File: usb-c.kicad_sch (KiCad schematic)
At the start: 10 parts, among them IC1 TCPP01-M12, IC2 USBLC6-2SC6, IC3 632723100011, Q1 STL11N3LLH6

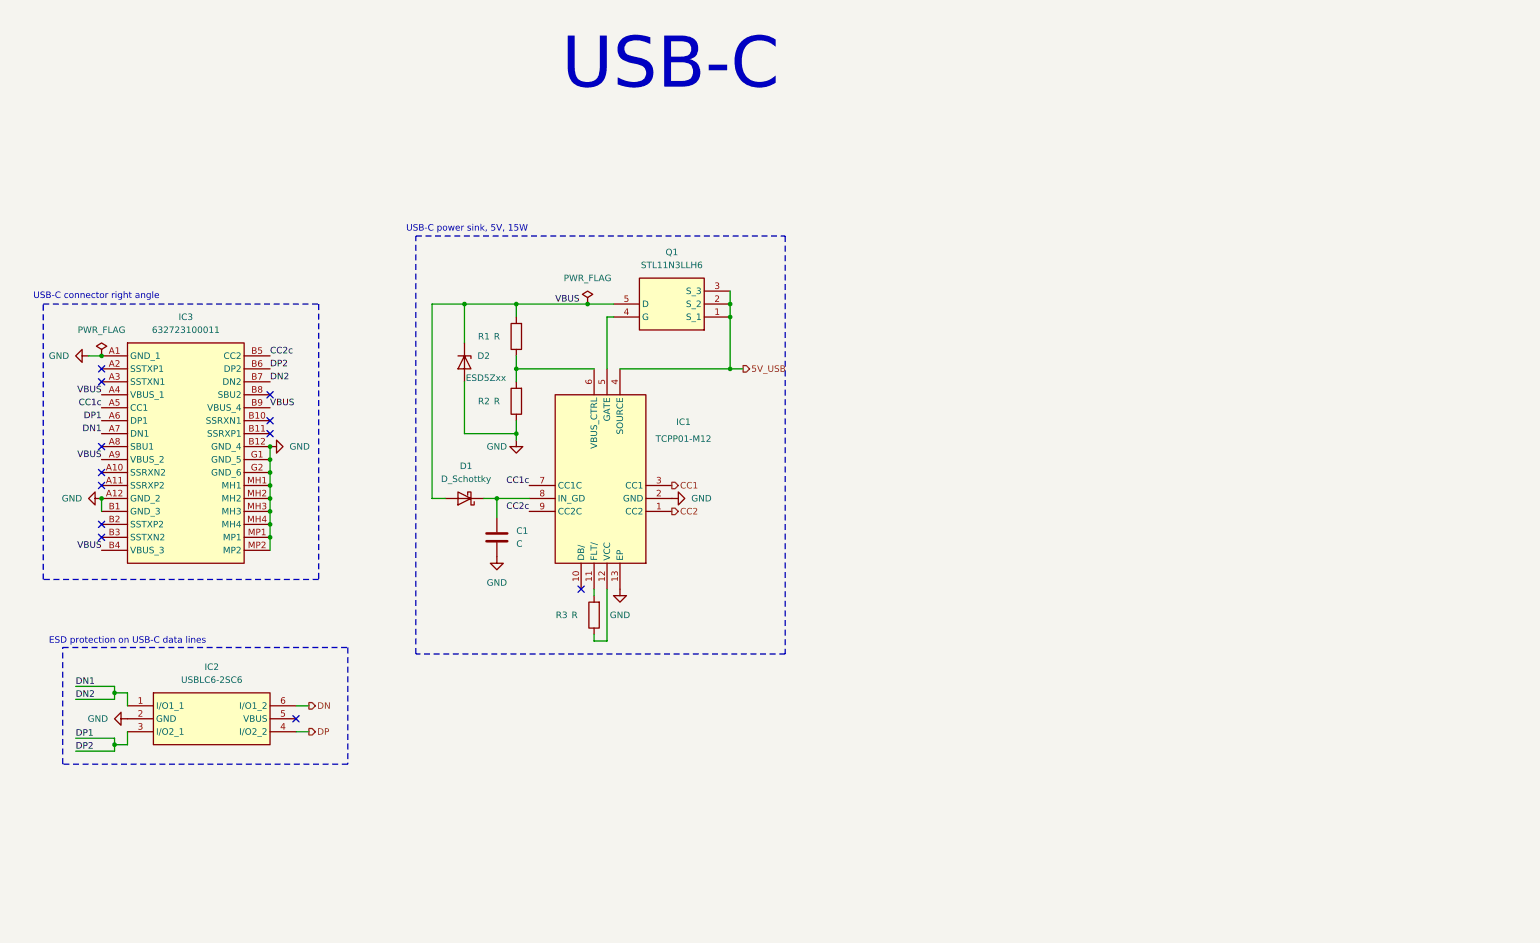
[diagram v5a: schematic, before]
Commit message: Connect all pins to MCU
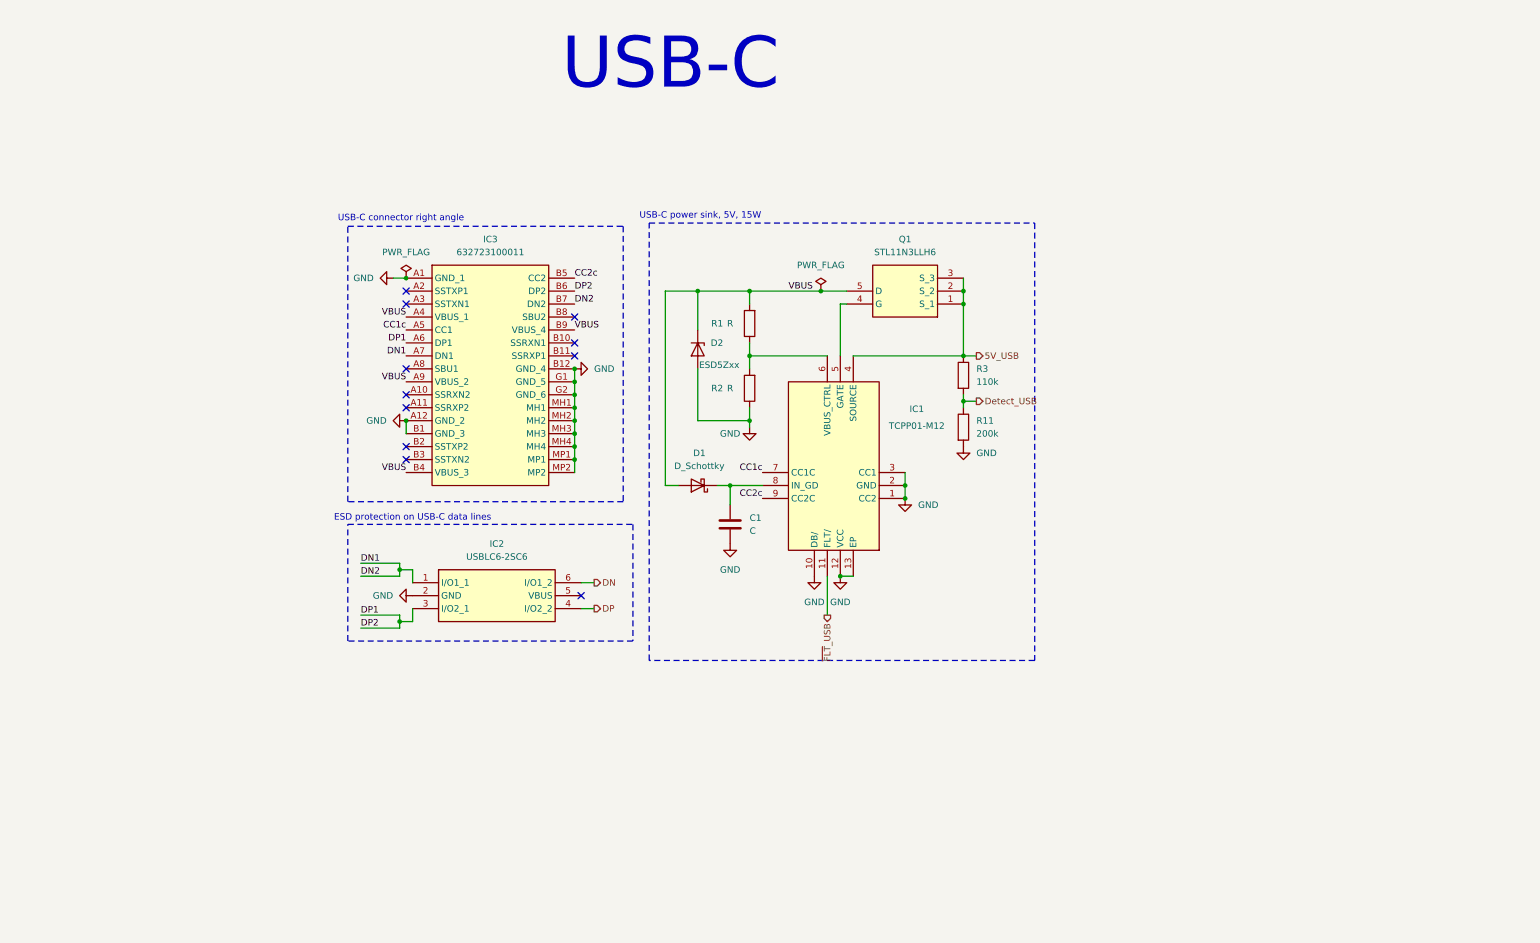
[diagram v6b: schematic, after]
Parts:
- added R11: 200k, symbol Device:R
- R3: value R -> 110k; footprint Resistor_SMD:R_0603_1608Metric_Pad0.98x0.95mm_HandSolder -> (none)
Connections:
- net CC1 is gone; now on net GND: IC1.3 (CC1)
- net CC2 is gone; now on net GND: IC1.1 (CC2)
- net 5V_USB: now also R3.1
- net GND: now also IC1.10 (DB/), IC1.12 (VCC), R11.2
- net Detect_USB: now reaches R3.2
- net Detect_USB: now also R11.1; no longer IC1.11 (FLT/)
- new net ~{FLT}_USB: IC1.11 (FLT/)
- no-connect marks 12 -> 11
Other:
- moved on the sheet: C1, D1, D2, IC1, IC2, IC3, Q1, R1, R2

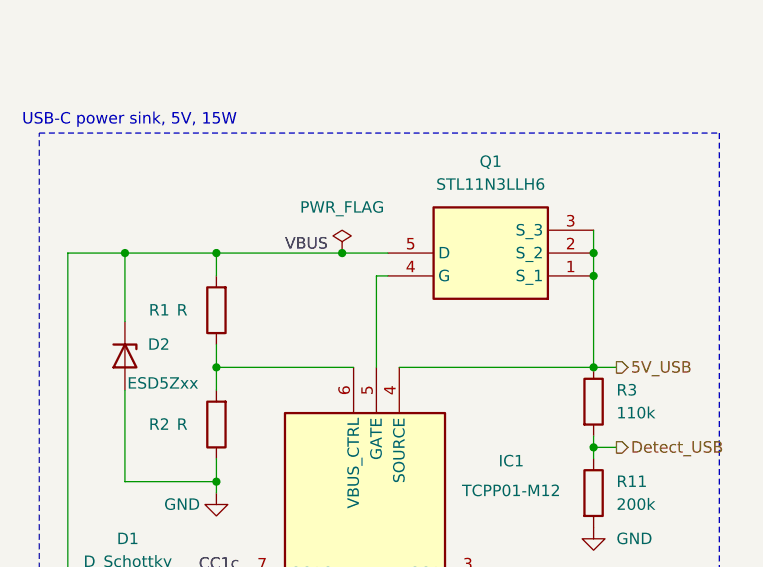
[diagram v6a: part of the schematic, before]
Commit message: Fix some ERC errors
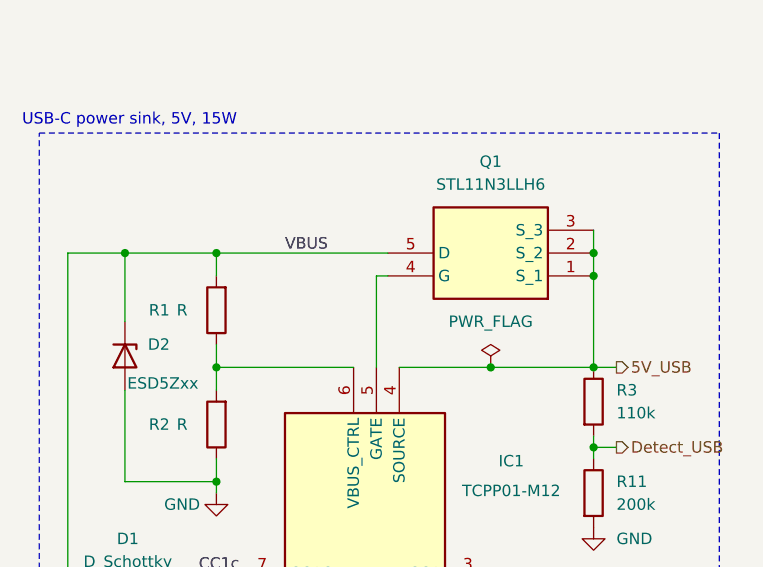
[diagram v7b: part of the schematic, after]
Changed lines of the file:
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@@
+	)
+	(junction
+		(at 191.77 81.28)
+		(diameter 0)
+		(color 0 0 0 0)
 	)
 	(junction
@@
 	)
 	(junction
-		(at 175.26 68.58)
-		(diameter 0)
-		(color 0 0 0 0)
-	)
-	(junction
 		(at 127 83.82)
 		(diameter 0)
@@
 	(wire
 		(pts
-			(xy 175.26 68.58) (xy 180.34 68.58)
-		)
-		(stroke
-			(width 0)
-			(type default)
-		)
-	)
-	(wire
-		(pts
 			(xy 179.07 71.12) (xy 180.34 71.12)
 		)
@@
 	(wire
 		(pts
-			(xy 161.29 68.58) (xy 175.26 68.58)
+			(xy 161.29 68.58) (xy 180.34 68.58)
 		)
 		(stroke
@@
 	(wire
 		(pts
-			(xy 181.61 81.28) (xy 203.2 81.28)
+			(xy 181.61 81.28) (xy 191.77 81.28)
 		)
 		(stroke
@@
 		(pts
 			(xy 151.13 83.82) (xy 151.13 93.98)
+		)
+		(stroke
+			(width 0)
+			(type default)
+		)
+	)
+	(wire
+		(pts
+			(xy 191.77 81.28) (xy 203.2 81.28)
 		)
 		(stroke
@@
 	(symbol
 		(lib_id "power:PWR_FLAG")
-		(at 175.26 68.58 0)
+		(at 191.77 81.28 0)
 		(unit 1)
 		(exclude_from_sim no)
@@
 		(fields_autoplaced yes)
 		(property "Reference" "#FLG01"
-			(at 175.26 66.675 0)
+			(at 191.77 79.375 0)
 			(effects
 				(font
@@
 		)
 		(property "Value" "PWR_FLAG"
-			(at 175.26 63.5 0)
+			(at 191.77 76.2 0)
 			(effects
 				(font
@@
 		)
 		(property "Footprint" ""
-			(at 175.26 68.58 0)
+			(at 191.77 81.28 0)
 			(effects
 				(font
@@
 		)
 		(property "Datasheet" "~"
-			(at 175.26 68.58 0)
+			(at 191.77 81.28 0)
 			(effects
 				(font
@@
 		)
 		(property "Description" "Special symbol for telling ERC where power comes from"
-			(at 175.26 68.58 0)
+			(at 191.77 81.28 0)
 			(effects
 				(font
@@
 		)
 		(instances
-			(project ""
+			(project "weather-station-poc"
 				(path "/38eb53bb-294e-46e4-ad59-fd355ca373b9/336d3e95-9b5f-4d37-8b5a-efff814cf96e"
 					(reference "#FLG01")

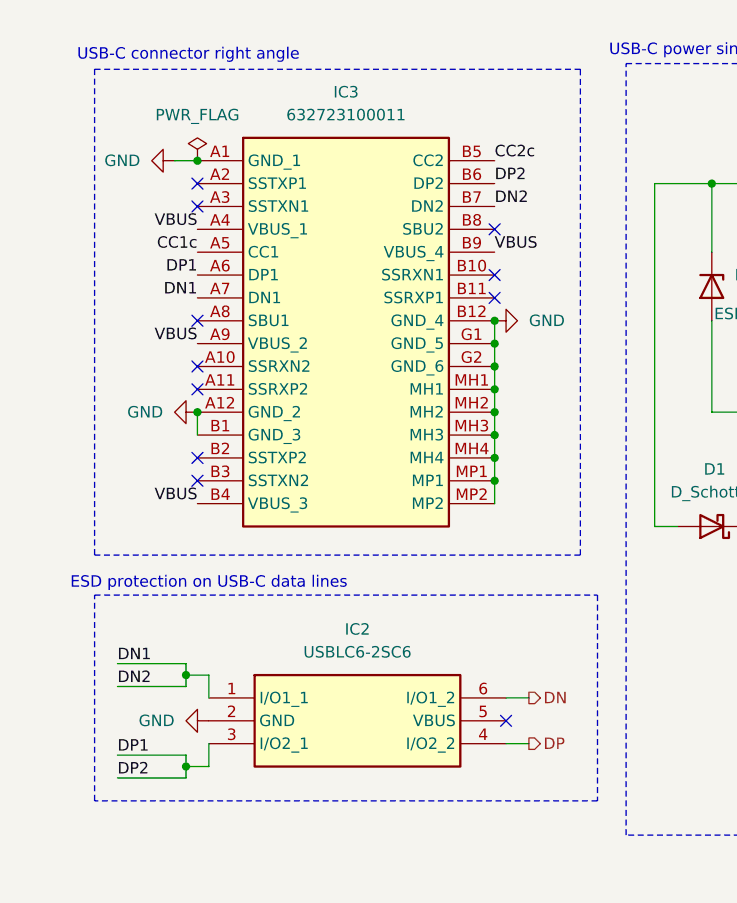
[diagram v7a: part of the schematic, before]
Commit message: Fix warnings for footprint
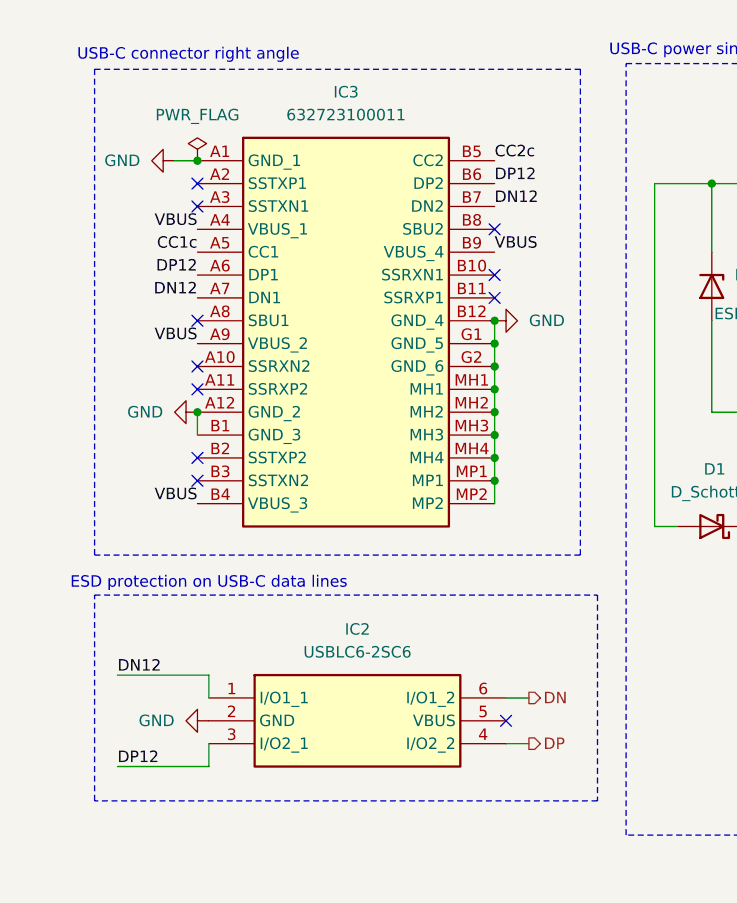
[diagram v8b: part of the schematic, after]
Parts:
- IC1: footprint QFN50P300X300X100-13N-D -> weather-station-poc-fp:QFN50P300X300X100-13N-D
- IC2: footprint SOT95P280X145-6N -> weather-station-poc-fp:SOT95P280X145-6N
- IC3: footprint 632723100011 -> weather-station-poc-fp:632723100011
- Q1: footprint STL20N6F7 -> weather-station-poc-fp:STL20N6F7
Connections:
- net DN1 renamed DN12
- net DP1 renamed DP12
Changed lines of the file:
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@@
-	)
-	(junction
-		(at 92.71 123.19)
-		(diameter 0)
-		(color 0 0 0 0)
-	)
-	(junction
-		(at 92.71 133.35)
-		(diameter 0)
-		(color 0 0 0 0)
 	)
 	(junction
@@
 	(wire
 		(pts
-			(xy 92.71 124.46) (xy 92.71 123.19)
-		)
-		(stroke
-			(width 0)
-			(type default)
-		)
-	)
-	(wire
-		(pts
 			(xy 161.29 95.25) (xy 161.29 93.98)
 		)
@@
 	(wire
 		(pts
-			(xy 85.09 134.62) (xy 92.71 134.62)
-		)
-		(stroke
-			(width 0)
-			(type default)
-		)
-	)
-	(wire
-		(pts
 			(xy 179.07 71.12) (xy 180.34 71.12)
 		)
@@
 	(wire
 		(pts
-			(xy 85.09 124.46) (xy 92.71 124.46)
-		)
-		(stroke
-			(width 0)
-			(type default)
-		)
-	)
-	(wire
-		(pts
 			(xy 161.29 81.28) (xy 176.53 81.28)
 		)
@@
 	(wire
 		(pts
-			(xy 92.71 133.35) (xy 95.25 133.35)
-		)
-		(stroke
-			(width 0)
-			(type default)
-		)
-	)
-	(wire
-		(pts
 			(xy 93.98 93.98) (xy 93.98 96.52)
 		)
@@
 	(wire
 		(pts
-			(xy 85.09 132.08) (xy 92.71 132.08)
+			(xy 85.09 133.35) (xy 95.25 133.35)
 		)
 		(stroke
@@
 	(wire
 		(pts
-			(xy 95.25 123.19) (xy 92.71 123.19)
+			(xy 85.09 123.19) (xy 95.25 123.19)
 		)
 		(stroke
@@
 	(wire
 		(pts
-			(xy 85.09 121.92) (xy 92.71 121.92)
-		)
-		(stroke
-			(width 0)
-			(type default)
-		)
-	)
-	(wire
-		(pts
 			(xy 161.29 78.74) (xy 161.29 81.28)
 		)
@@
 	(wire
 		(pts
-			(xy 92.71 123.19) (xy 92.71 121.92)
-		)
-		(stroke
-			(width 0)
-			(type default)
-		)
-	)
-	(wire
-		(pts
 			(xy 203.2 81.28) (xy 205.74 81.28)
 		)
@@
 	(wire
 		(pts
-			(xy 92.71 134.62) (xy 92.71 133.35)
-		)
-		(stroke
-			(width 0)
-			(type default)
-		)
-	)
-	(wire
-		(pts
-			(xy 92.71 132.08) (xy 92.71 133.35)
-		)
-		(stroke
-			(width 0)
-			(type default)
-		)
-	)
-	(wire
-		(pts
 			(xy 144.78 68.58) (xy 151.13 68.58)
 		)
@@
 		)
 	)
-	(label "DN2"
+	(label "DN12"
 		(at 127 71.12 0)
 		(effects
@@
 		)
 	)
-	(label "DP2"
+	(label "DP12"
 		(at 127 68.58 0)
 		(effects
@@
 		)
 	)
-	(label "DN2"
-		(at 85.09 124.46 0)
-		(effects
-			(font
-				(size 1.27 1.27)
-			)
-			(justify left bottom)
-		)
-	)
-	(label "DP1"
+	(label "DP12"
 		(at 93.98 78.74 180)
 		(effects
@@
 		)
 	)
-	(label "DN1"
+	(label "DN12"
 		(at 93.98 81.28 180)
 		(effects
@@
 			)
 			(justify right bottom)
-		)
-	)
-	(label "DN1"
-		(at 85.09 121.92 0)
-		(effects
-			(font
-				(size 1.27 1.27)
-			)
-			(justify left bottom)
 		)
 	)
@@
 		)
 	)
-	(label "DP2"
-		(at 85.09 134.62 0)
-		(effects
-			(font
-				(size 1.27 1.27)
-			)
-			(justify left bottom)
-		)
-	)
 	(label "CC1c"
 		(at 163.83 104.14 180)
@@
 		)
 	)
-	(label "DP1"
-		(at 85.09 132.08 0)
+	(label "DN12"
+		(at 85.09 123.19 0)
+		(effects
+			(font
+				(size 1.27 1.27)
+			)
+			(justify left bottom)
+		)
+	)
+	(label "DP12"
+		(at 85.09 133.35 0)
 		(effects
 			(font
@@
 			)
 		)
-		(property "Footprint" "632723100011"
+		(property "Footprint" "weather-station-poc-fp:632723100011"
 			(at 123.19 160.96 0)
 			(effects
@@
 			)
 		)
-		(property "Footprint" "STL20N6F7"
+		(property "Footprint" "weather-station-poc-fp:STL20N6F7"
 			(at 184.15 -23.8 0)
 			(effects
@@
 			)
 		)
-		(property "Footprint" "QFN50P300X300X100-13N-D"
+		(property "Footprint" "weather-station-poc-fp:QFN50P300X300X100-13N-D"
 			(at 167.64 21.92 0)
 			(effects
@@
 			)
 		)
-		(property "Footprint" "SOT95P280X145-6N"
+		(property "Footprint" "weather-station-poc-fp:SOT95P280X145-6N"
 			(at 124.46 220.65 0)
 			(effects
